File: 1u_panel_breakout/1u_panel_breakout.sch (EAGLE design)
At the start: 3 parts, among them J1 1734354-1

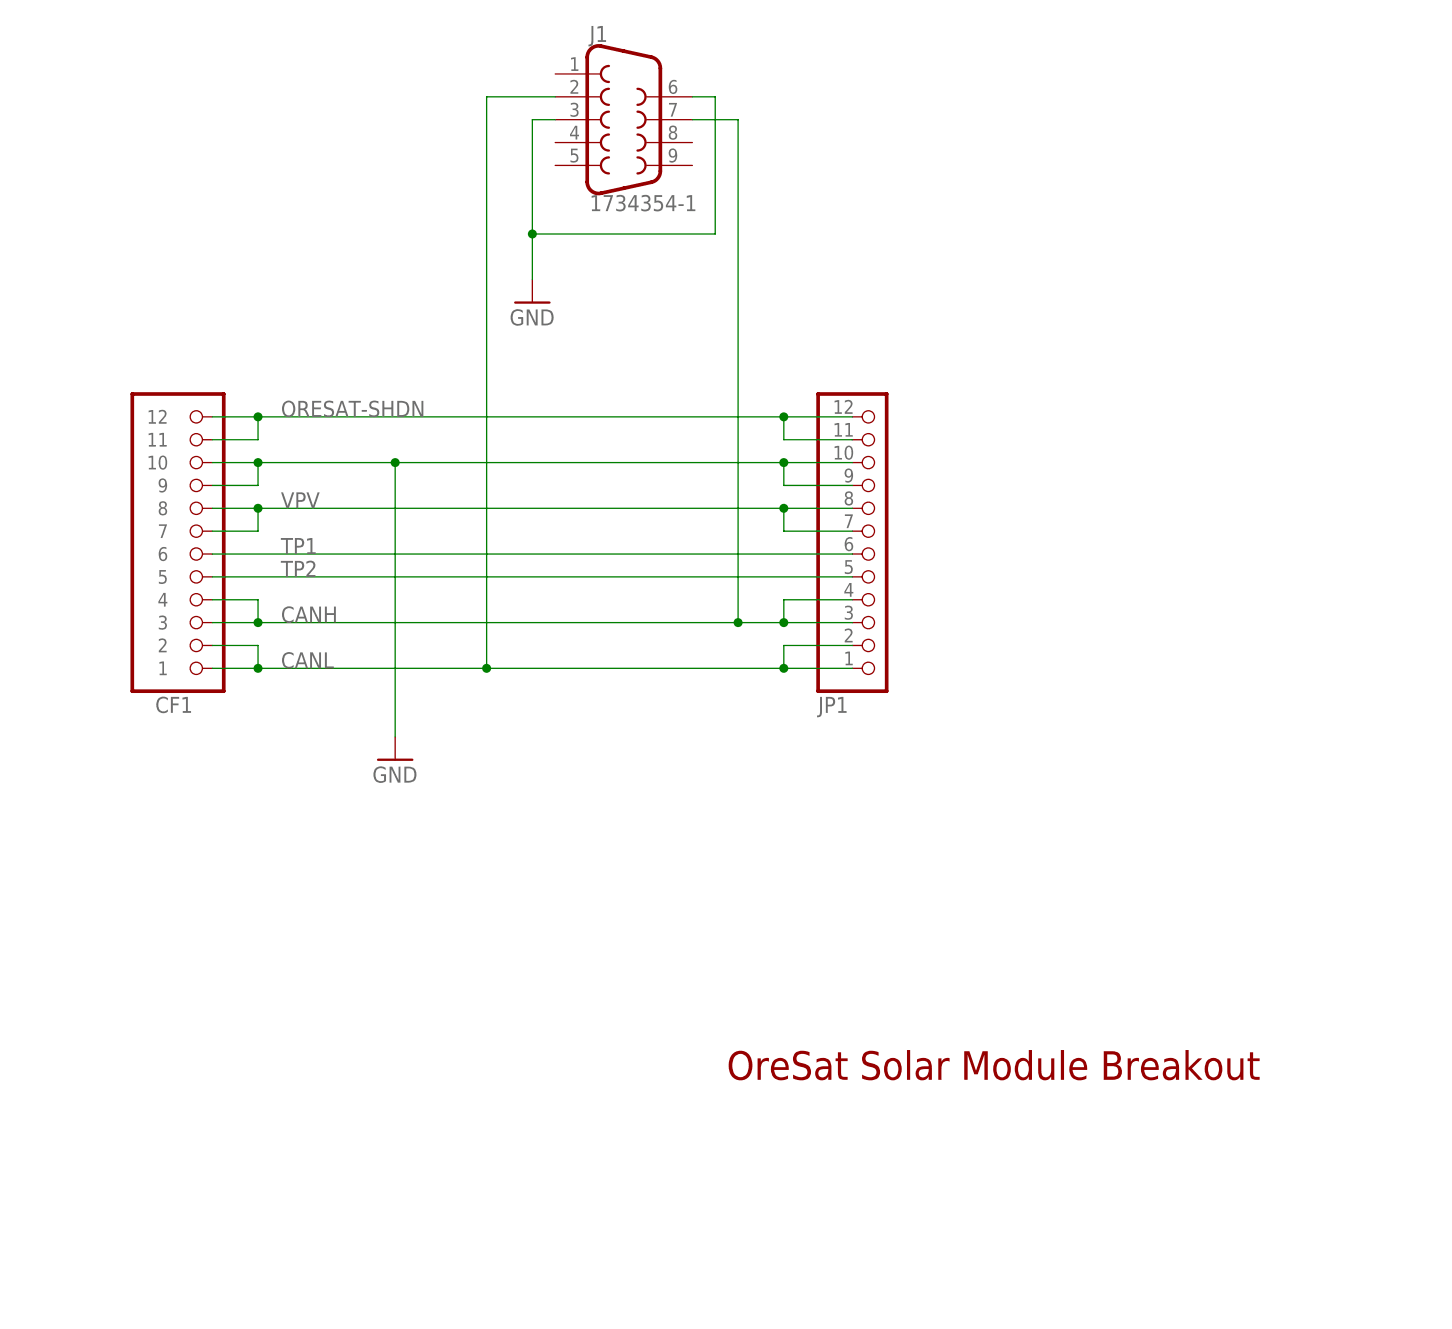
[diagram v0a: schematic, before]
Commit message: Fixed breakout connector to solar panel, added scope clips.
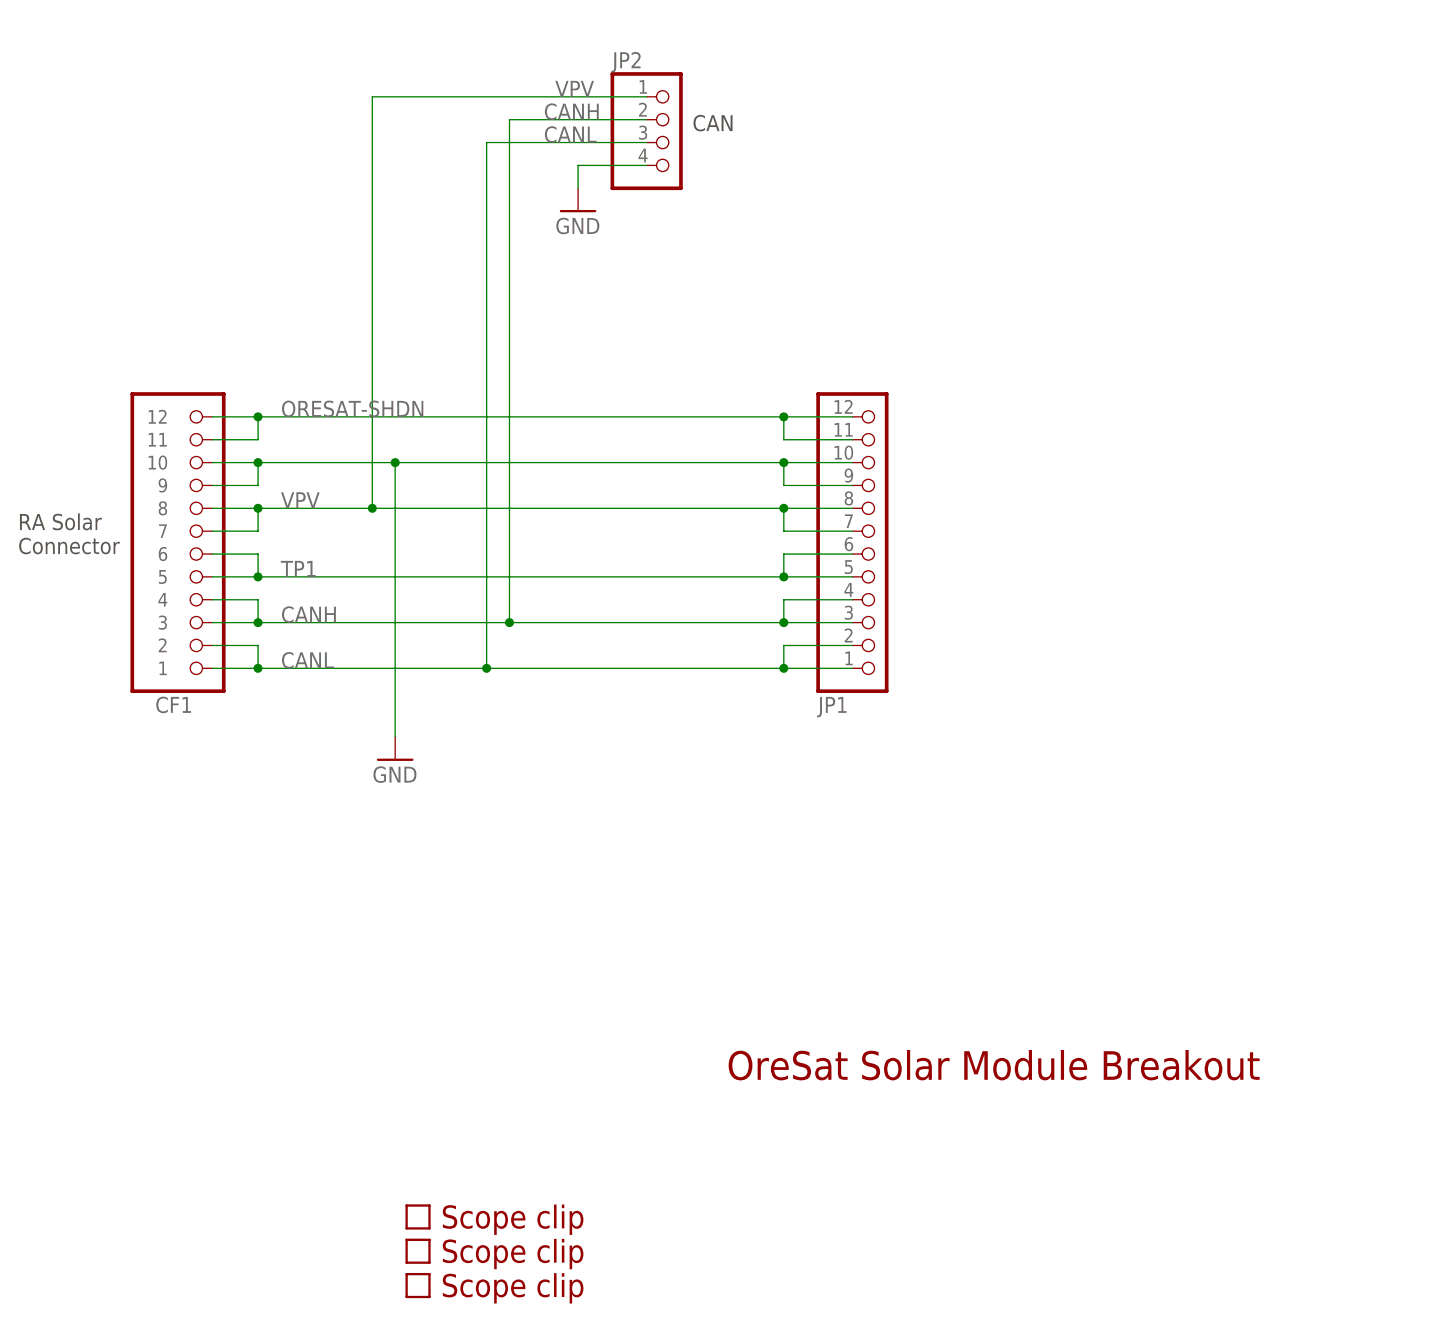
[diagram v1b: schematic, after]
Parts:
- removed J1: 1734354-1, TE_Conn_DE9:TE_DE9_RECEPTACLE1734354-1
- added JP2: (no value), pinhead:PINHD-1X4
- added U$1, U$2, U$3: SCOPE_CLIP, oresat-misc:SCOPE_CLIP
- CF1: value ORESAT-SOLARPANEL-12PIN -> ORESAT-SOLARPANEL-CARD-12PIN; device oresat-eagle:ORESAT-SOLARPANEL-12PIN -> oresat-connectors:ORESAT-SOLARPANEL-CARD-12PIN
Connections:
- removed net TP2: CF1.5, JP1.5
- net CANH: now also JP2.2; no longer J1.7
- net CANL: now also JP2.3; no longer J1.2
- net GND: now also JP2.4; no longer J1.3, J1.6
- net TP1: now also CF1.5, JP1.5
- net VPV: now also JP2.1
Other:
- note added: "CAN"
- note added: "RA Solar Connector"
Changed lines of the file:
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@@
 <?xml version="1.0" encoding="utf-8"?>
 <!DOCTYPE eagle SYSTEM "eagle.dtd">
-<eagle version="7.6.0">
+<eagle version="8.6.0">
 <drawing>
 <settings>
 <setting alwaysvectorfont="no"/>
+<setting keepoldvectorfont="yes"/>
 <setting verticaltext="up"/>
 </settings>
-<grid distance="0.05" unitdist="inch" unit="inch" style="lines" multiple="1" display="yes" altdistance="0.005" altunitdist="inch" altunit="inch"/>
+<grid distance="0.05" unitdist="inch" unit="inch" style="lines" multiple="2" display="no" altdistance="0.01" altunitdist="inch" altunit="inch"/>
 <layers>
 <layer number="1" name="Top" color="4" fill="1" visible="no" active="no"/>
+<layer number="2" name="Route2" color="1" fill="3" visible="no" active="no"/>
+<layer number="3" name="Route3" color="4" fill="3" visible="no" active="no"/>
+<layer number="4" name="Route4" color="1" fill="4" visible="no" active="no"/>
+<layer number="5" name="Route5" color="4" fill="4" visible="no" active="no"/>
+<layer number="6" name="Route6" color="1" fill="8" visible="no" active="no"/>
+<layer number="7" name="Route7" color="4" fill="8" visible="no" active="no"/>
+<layer number="8" name="Route8" color="1" fill="2" visible="no" active="no"/>
+<layer number="9" name="Route9" color="4" fill="2" visible="no" active="no"/>
+<layer number="10" name="Route10" color="1" fill="7" visible="no" active="no"/>
+<layer number="11" name="Route11" color="4" fill="7" visible="no" active="no"/>
+<layer number="12" name="Route12" color="1" fill="5" visible="no" active="no"/>
+<layer number="13" name="Route13" color="4" fill="5" visible="no" active="no"/>
+<layer number="14" name="Route14" color="1" fill="6" visible="no" active="no"/>
+<layer number="15" name="Route15" color="4" fill="6" visible="no" active="no"/>
 <layer number="16" name="Bottom" color="1" fill="1" visible="no" active="no"/>
 <layer number="17" name="Pads" color="2" fill="1" visible="no" active="no"/>
@@
 <parts>
 <part name="FRAME1" library="frames" deviceset="LETTER_L" device=""/>
-<part name="CF1" library="oresat-eagle" deviceset="ORESAT-SOLARPANEL-12PIN" device=""/>
+<part name="CF1" library="oresat-connectors" deviceset="ORESAT-SOLARPANEL-CARD-12PIN" device=""/>
 <part name="JP1" library="pinhead" deviceset="PINHD-1X12" device=""/>
 <part name="GND1" library="supply1" deviceset="GND" device=""/>
 <part name="GND2" library="supply1" deviceset="GND" device=""/>
-<part name="J1" library="TE_Conn_DE9" deviceset="TE_DE9_RECEPTACLE" device="1734354-1" value="1734354-1"/>
+<part name="JP2" library="pinhead" library_urn="urn:adsk.eagle:library:325" deviceset="PINHD-1X4" device="" package3d_urn="urn:adsk.eagle:package:22407/2"/>
+<part name="U$1" library="oresat-misc" deviceset="SCOPE_CLIP" device=""/>
+<part name="U$2" library="oresat-misc" deviceset="SCOPE_CLIP" device=""/>
+<part name="U$3" library="oresat-misc" deviceset="SCOPE_CLIP" device=""/>
 </parts>
 <sheets>
@@
 <plain>
 <text x="115.57" y="-20.32" size="3.175" layer="94">OreSat Solar Module Breakout</text>
+<text x="36.83" y="38.1" size="1.778" layer="97">RA Solar
+Connector</text>
+<text x="111.76" y="85.09" size="1.778" layer="97">CAN</text>
 </plain>
 <instances>
@@
 <instance part="JP1" gate="G$1" x="132.08" y="38.1" rot="MR180"/>
 <instance part="GND1" gate="1" x="78.74" y="15.24"/>
-<instance part="GND2" gate="1" x="93.98" y="66.04"/>
-<instance part="J1" gate="G$1" x="104.14" y="86.36"/>
+<instance part="GND2" gate="1" x="99.06" y="76.2"/>
+<instance part="JP2" gate="A" x="109.22" y="83.82"/>
+<instance part="U$1" gate="G$1" x="81.28" y="-43.18"/>
+<instance part="U$2" gate="G$1" x="81.28" y="-39.37"/>
+<instance part="U$3" gate="G$1" x="81.28" y="-35.56"/>
 </instances>
 <busses>
@@
 <junction x="63.5" y="25.4"/>
 <label x="66.04" y="25.4" size="1.778" layer="95"/>
-<wire x1="96.52" y1="88.9" x2="88.9" y2="88.9" width="0.1524" layer="91"/>
-<wire x1="88.9" y1="88.9" x2="88.9" y2="25.4" width="0.1524" layer="91"/>
 <junction x="88.9" y="25.4"/>
-<pinref part="J1" gate="G$1" pin="2"/>
+<pinref part="JP2" gate="A" pin="3"/>
+<wire x1="88.9" y1="83.82" x2="88.9" y2="25.4" width="0.1524" layer="91"/>
+<wire x1="106.68" y1="83.82" x2="88.9" y2="83.82" width="0.1524" layer="91"/>
+<label x="95.25" y="83.82" size="1.778" layer="95"/>
 </segment>
 </net>
@@
 <wire x1="58.42" y1="30.48" x2="63.5" y2="30.48" width="0.1524" layer="91"/>
 <pinref part="JP1" gate="G$1" pin="4"/>
-<wire x1="63.5" y1="30.48" x2="116.84" y2="30.48" width="0.1524" layer="91"/>
-<wire x1="116.84" y1="30.48" x2="121.92" y2="30.48" width="0.1524" layer="91"/>
+<wire x1="63.5" y1="30.48" x2="91.44" y2="30.48" width="0.1524" layer="91"/>
+<wire x1="91.44" y1="30.48" x2="121.92" y2="30.48" width="0.1524" layer="91"/>
 <wire x1="121.92" y1="30.48" x2="129.54" y2="30.48" width="0.1524" layer="91"/>
 <wire x1="129.54" y1="33.02" x2="121.92" y2="33.02" width="0.1524" layer="91"/>
@@
 <junction x="63.5" y="30.48"/>
 <label x="66.04" y="30.48" size="1.778" layer="95"/>
-<wire x1="111.76" y1="86.36" x2="116.84" y2="86.36" width="0.1524" layer="91"/>
-<wire x1="116.84" y1="86.36" x2="116.84" y2="30.48" width="0.1524" layer="91"/>
-<junction x="116.84" y="30.48"/>
-<pinref part="J1" gate="G$1" pin="7"/>
+<wire x1="91.44" y1="86.36" x2="91.44" y2="30.48" width="0.1524" layer="91"/>
+<junction x="91.44" y="30.48"/>
+<pinref part="JP2" gate="A" pin="2"/>
+<wire x1="91.44" y1="86.36" x2="106.68" y2="86.36" width="0.1524" layer="91"/>
+<label x="95.25" y="86.36" size="1.778" layer="95"/>
 </segment>
 </net>
@@
 <wire x1="58.42" y1="43.18" x2="63.5" y2="43.18" width="0.1524" layer="91"/>
 <pinref part="JP1" gate="G$1" pin="7"/>
-<wire x1="63.5" y1="43.18" x2="121.92" y2="43.18" width="0.1524" layer="91"/>
+<wire x1="63.5" y1="43.18" x2="76.2" y2="43.18" width="0.1524" layer="91"/>
+<wire x1="76.2" y1="43.18" x2="121.92" y2="43.18" width="0.1524" layer="91"/>
 <wire x1="121.92" y1="43.18" x2="129.54" y2="43.18" width="0.1524" layer="91"/>
 <wire x1="129.54" y1="40.64" x2="121.92" y2="40.64" width="0.1524" layer="91"/>
@@
 <junction x="63.5" y="43.18"/>
 <label x="66.04" y="43.18" size="1.778" layer="95"/>
+<wire x1="76.2" y1="43.18" x2="76.2" y2="88.9" width="0.1524" layer="91"/>
+<junction x="76.2" y="43.18"/>
+<pinref part="JP2" gate="A" pin="1"/>
+<wire x1="76.2" y1="88.9" x2="106.68" y2="88.9" width="0.1524" layer="91"/>
+<label x="96.52" y="88.9" size="1.778" layer="95"/>
 </segment>
 </net>
 <net name="TP1" class="0">
 <segment>
+<pinref part="JP1" gate="G$1" pin="5"/>
+<pinref part="CF1" gate="G$1" pin="5"/>
+<wire x1="129.54" y1="35.56" x2="121.92" y2="35.56" width="0.1524" layer="91"/>
 <pinref part="CF1" gate="G$1" pin="6"/>
 <pinref part="JP1" gate="G$1" pin="6"/>
-<wire x1="58.42" y1="38.1" x2="129.54" y2="38.1" width="0.1524" layer="91"/>
-<label x="66.04" y="38.1" size="1.778" layer="95"/>
-</segment>
-</net>
-<net name="TP2" class="0">
-<segment>
-<pinref part="JP1" gate="G$1" pin="5"/>
-<pinref part="CF1" gate="G$1" pin="5"/>
-<wire x1="129.54" y1="35.56" x2="58.42" y2="35.56" width="0.1524" layer="91"/>
+<wire x1="63.5" y1="35.56" x2="58.42" y2="35.56" width="0.1524" layer="91"/>
+<wire x1="58.42" y1="38.1" x2="63.5" y2="38.1" width="0.1524" layer="91"/>
 <label x="66.04" y="35.56" size="1.778" layer="95"/>
+<wire x1="121.92" y1="38.1" x2="129.54" y2="38.1" width="0.1524" layer="91"/>
+<wire x1="63.5" y1="35.56" x2="63.5" y2="38.1" width="0.1524" layer="91"/>
+<wire x1="121.92" y1="38.1" x2="121.92" y2="35.56" width="0.1524" layer="91"/>
+<wire x1="63.5" y1="35.56" x2="121.92" y2="35.56" width="0.1524" layer="91"/>
+<junction x="63.5" y="35.56"/>
+<junction x="121.92" y="35.56"/>
 </segment>
 </net>
 <net name="GND" class="0">
-<segment>
-<pinref part="GND2" gate="1" pin="GND"/>
-<wire x1="93.98" y1="68.58" x2="93.98" y2="73.66" width="0.1524" layer="91"/>
-<wire x1="93.98" y1="73.66" x2="93.98" y2="86.36" width="0.1524" layer="91"/>
-<wire x1="111.76" y1="88.9" x2="114.3" y2="88.9" width="0.1524" layer="91"/>
-<wire x1="114.3" y1="88.9" x2="114.3" y2="73.66" width="0.1524" layer="91"/>
-<wire x1="114.3" y1="73.66" x2="93.98" y2="73.66" width="0.1524" layer="91"/>
-<junction x="93.98" y="73.66"/>
-<wire x1="93.98" y1="86.36" x2="96.52" y2="86.36" width="0.1524" layer="91"/>
-<pinref part="J1" gate="G$1" pin="6"/>
-<pinref part="J1" gate="G$1" pin="3"/>
-</segment>
 <segment>
 <pinref part="CF1" gate="G$1" pin="10"/>
@@
 <junction x="78.74" y="48.26"/>
 </segment>
+<segment>
+<pinref part="GND2" gate="1" pin="GND"/>
+<wire x1="99.06" y1="78.74" x2="99.06" y2="81.28" width="0.1524" layer="91"/>
+<pinref part="JP2" gate="A" pin="4"/>
+<wire x1="99.06" y1="81.28" x2="106.68" y2="81.28" width="0.1524" layer="91"/>
+</segment>
 </net>
 </nets>
 </sheet>
 </sheets>
+<errors>
+</errors>
 </schematic>
 </drawing>
+<compatibility>
+<note version="6.3" minversion="6.2.2" severity="warning">
+Since Version 6.2.2 text objects can contain more than one line,
+which will not be processed correctly with this version.
+</note>
+<note version="8.2" severity="warning">
+Since Version 8.2, EAGLE supports online libraries. The ids
+of those online libraries will not be understood (or retained)
+with this version.
+</note>
+<note version="8.3" severity="warning">
+Since Version 8.3, EAGLE supports URNs for individual library
+assets (packages, symbols, and devices). The URNs of those assets
+will not be understood (or retained) with this version.
+</note>
+<note version="8.3" severity="warning">
+Since Version 8.3, EAGLE supports the association of 3D packages
+with devices in libraries, schematics, and board files. Those 3D
+packages will not be understood (or retained) with this version.
+</note>
+</compatibility>
 </eagle>

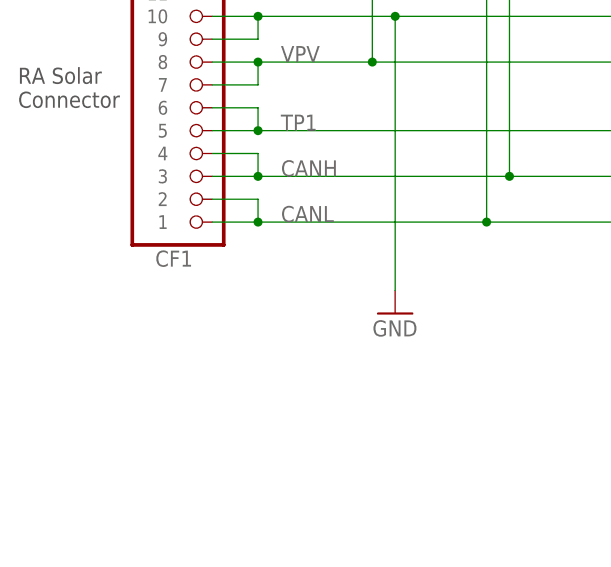
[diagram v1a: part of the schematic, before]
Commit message: Added part numbers to odd connectors.
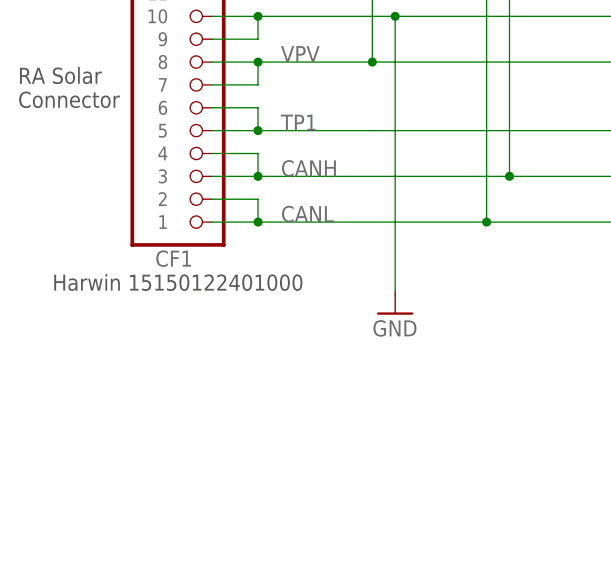
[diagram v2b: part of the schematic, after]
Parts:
- CF1: value ORESAT-SOLARPANEL-CARD-12PIN -> 15150122401000
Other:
- note added: "Harwin 15150122401000"
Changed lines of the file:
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@@
 <setting verticaltext="up"/>
 </settings>
-<grid distance="0.05" unitdist="inch" unit="inch" style="lines" multiple="2" display="no" altdistance="0.01" altunitdist="inch" altunit="inch"/>
+<grid distance="0.1" unitdist="inch" unit="inch" style="lines" multiple="1" display="no" altdistance="0.01" altunitdist="inch" altunit="inch"/>
 <layers>
 <layer number="1" name="Top" color="4" fill="1" visible="no" active="no"/>
@@
 <parts>
 <part name="FRAME1" library="frames" deviceset="LETTER_L" device=""/>
-<part name="CF1" library="oresat-connectors" deviceset="ORESAT-SOLARPANEL-CARD-12PIN" device=""/>
+<part name="CF1" library="oresat-connectors" deviceset="ORESAT-SOLARPANEL-CARD-12PIN" device="" value="15150122401000"/>
 <part name="JP1" library="pinhead" deviceset="PINHD-1X12" device=""/>
 <part name="GND1" library="supply1" deviceset="GND" device=""/>
@@
 Connector</text>
 <text x="111.76" y="85.09" size="1.778" layer="97">CAN</text>
+<text x="40.64" y="17.78" size="1.778" layer="97">Harwin 15150122401000</text>
 </plain>
 <instances>
